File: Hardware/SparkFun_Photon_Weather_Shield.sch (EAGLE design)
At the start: 42 parts, among them U1 3.3V MIC5219, U2 HTU21D, U3 MPL3115A2LGA8

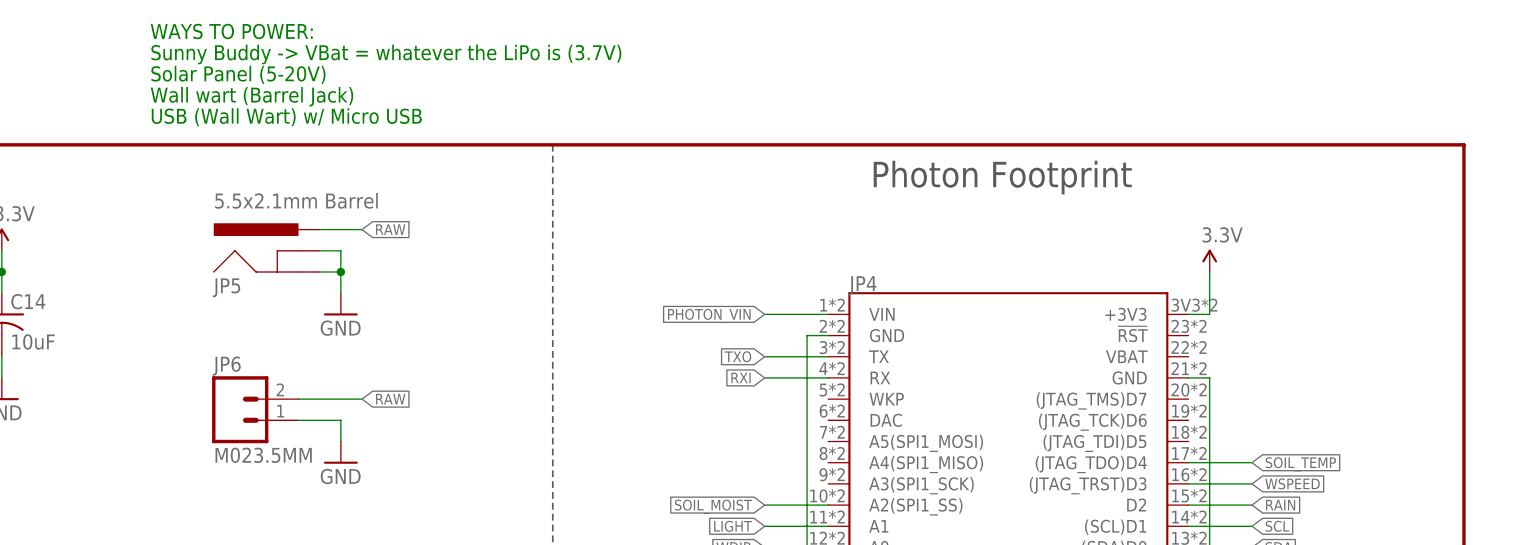
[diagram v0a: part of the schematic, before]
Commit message: Peer Review complete
Peer review with Jim, added 3.3V disable jumper for two power sources
at once (debugging), minor edits.
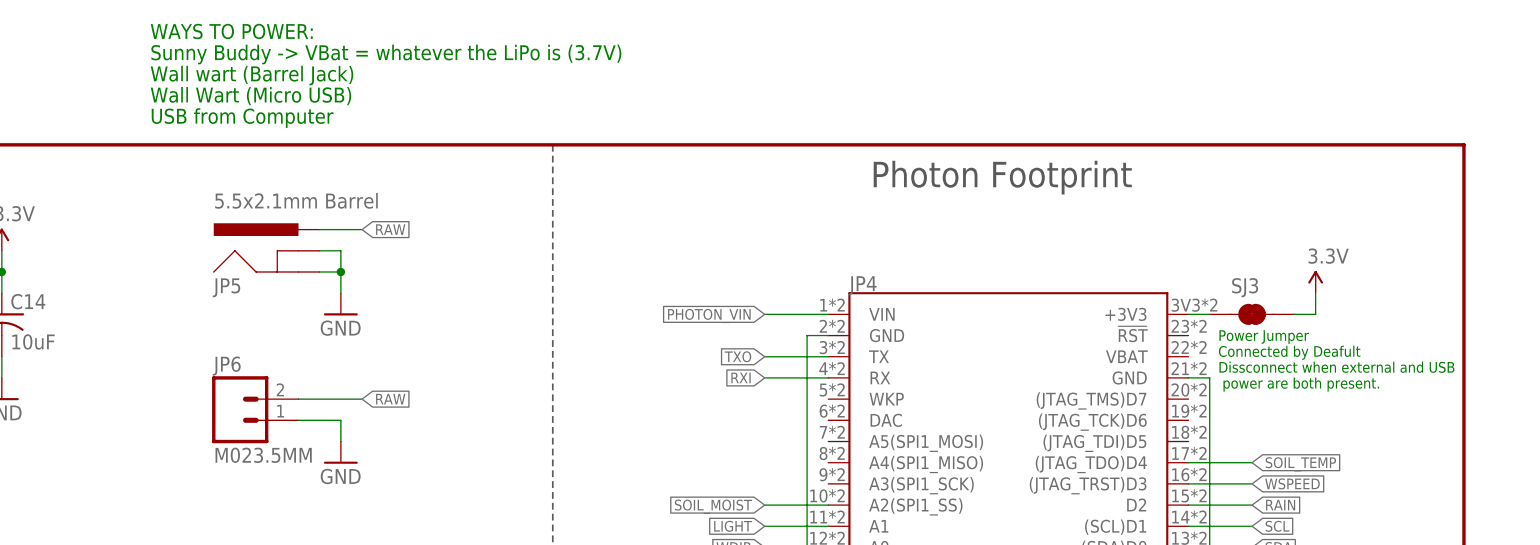
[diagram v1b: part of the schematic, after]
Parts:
- added SJ3: JUMPER-PAD-2-NC_BY_TRACE, SparkFun-Passives:JUMPER-PAD-2-NC_BY_TRACE
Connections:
- new net N$7: JP4.+3V3, SJ3.1
- net 3.3V: now also SJ3.2; no longer JP4.+3V3
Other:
- note added: "Power Jumper Connected by Deafult Dissconnect when external and USB power are both present."
- note added: "USB from Computer"
- note added: "Wall Wart (Micro USB)"
- note removed: "Solar Panel (5-20V)"
- note removed: "USB (Wall Wart) w/ Micro USB"
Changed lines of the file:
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@@
 <part name="FID2" library="SparkFun-Aesthetics" deviceset="FIDUCIAL" device="1X2"/>
 <part name="LOGO2" library="SparkFun-Aesthetics" deviceset="SFE_LOGO_NAME_FLAME" device=".1_INCH"/>
+<part name="SJ3" library="SparkFun-Passives" deviceset="JUMPER-PAD-2-NC_BY_TRACE" device="" value=""/>
 </parts>
 <sheets>
@@
 <text x="96.012" y="36.068" size="2.032" layer="102">I2C Port (optional)</text>
 <text x="91.44" y="195.58" size="1.778" layer="91">Sunny Buddy -&gt; VBat = whatever the LiPo is (3.7V)</text>
-<text x="91.44" y="193.04" size="1.778" layer="91">Solar Panel (5-20V)</text>
-<text x="91.44" y="190.5" size="1.778" layer="91">Wall wart (Barrel Jack)</text>
-<text x="91.44" y="187.96" size="1.778" layer="91">USB (Wall Wart) w/ Micro USB</text>
+<text x="91.44" y="187.96" size="1.778" layer="91">USB from Computer</text>
+<text x="91.44" y="193.04" size="1.778" layer="91">Wall wart (Barrel Jack)</text>
+<text x="91.44" y="190.5" size="1.778" layer="91">Wall Wart (Micro USB)</text>
 <text x="104.14" y="134.62" size="1.778" layer="91">Power Selection</text>
 <text x="91.44" y="198.12" size="1.778" layer="91">WAYS TO POWER:</text>
 <text x="149.86" y="7.62" size="1.778" layer="94" ratio="12">Based on the Weather Shield for Arduino by Nathan Seidle</text>
 <text x="27.94" y="144.78" size="1.778" layer="97">Min Voltage Input: 5VDC</text>
+<text x="219.456" y="156.21" size="1.27" layer="91">Power Jumper
+Connected by Deafult
+Dissconnect when external and USB
+ power are both present. </text>
 </plain>
 <instances>
@@
 </instance>
 <instance part="LOGO1" gate="G$1" x="165.1" y="45.72"/>
-<instance part="P+2" gate="G$1" x="218.44" y="170.18"/>
+<instance part="P+2" gate="G$1" x="231.14" y="167.64"/>
 <instance part="JP2" gate="G$1" x="7.62" y="17.78"/>
 <instance part="JP3" gate="G$1" x="55.88" y="17.78"/>
@@
 <instance part="FID2" gate="G$1" x="243.84" y="25.4"/>
 <instance part="LOGO2" gate="G$1" x="190.5" y="33.02"/>
+<instance part="SJ3" gate="G$1" x="223.52" y="165.1"/>
 </instances>
 <busses>
@@
 </segment>
 <segment>
-<pinref part="P+2" gate="G$1" pin="3.3V"/>
-<wire x1="215.9" y1="165.1" x2="218.44" y2="165.1" width="0.1524" layer="91"/>
-<wire x1="218.44" y1="165.1" x2="218.44" y2="170.18" width="0.1524" layer="91"/>
-<pinref part="JP4" gate="G$1" pin="+3V3"/>
-</segment>
-<segment>
 <pinref part="JP2" gate="G$1" pin="3"/>
 <wire x1="15.24" y1="20.32" x2="17.78" y2="20.32" width="0.1524" layer="91"/>
@@
 <pinref part="R17" gate="G$1" pin="1"/>
 <pinref part="P+14" gate="1" pin="VCC"/>
+</segment>
+<segment>
+<pinref part="SJ3" gate="G$1" pin="2"/>
+<pinref part="P+2" gate="G$1" pin="3.3V"/>
+<wire x1="231.14" y1="167.64" x2="231.14" y2="165.1" width="0.1524" layer="91"/>
+<wire x1="231.14" y1="165.1" x2="228.6" y2="165.1" width="0.1524" layer="91"/>
 </segment>
 </net>
@@
 </segment>
 </net>
+<net name="N$7" class="0">
+<segment>
+<pinref part="SJ3" gate="G$1" pin="1"/>
+<pinref part="JP4" gate="G$1" pin="+3V3"/>
+<wire x1="218.44" y1="165.1" x2="215.9" y2="165.1" width="0.1524" layer="91"/>
+</segment>
+</net>

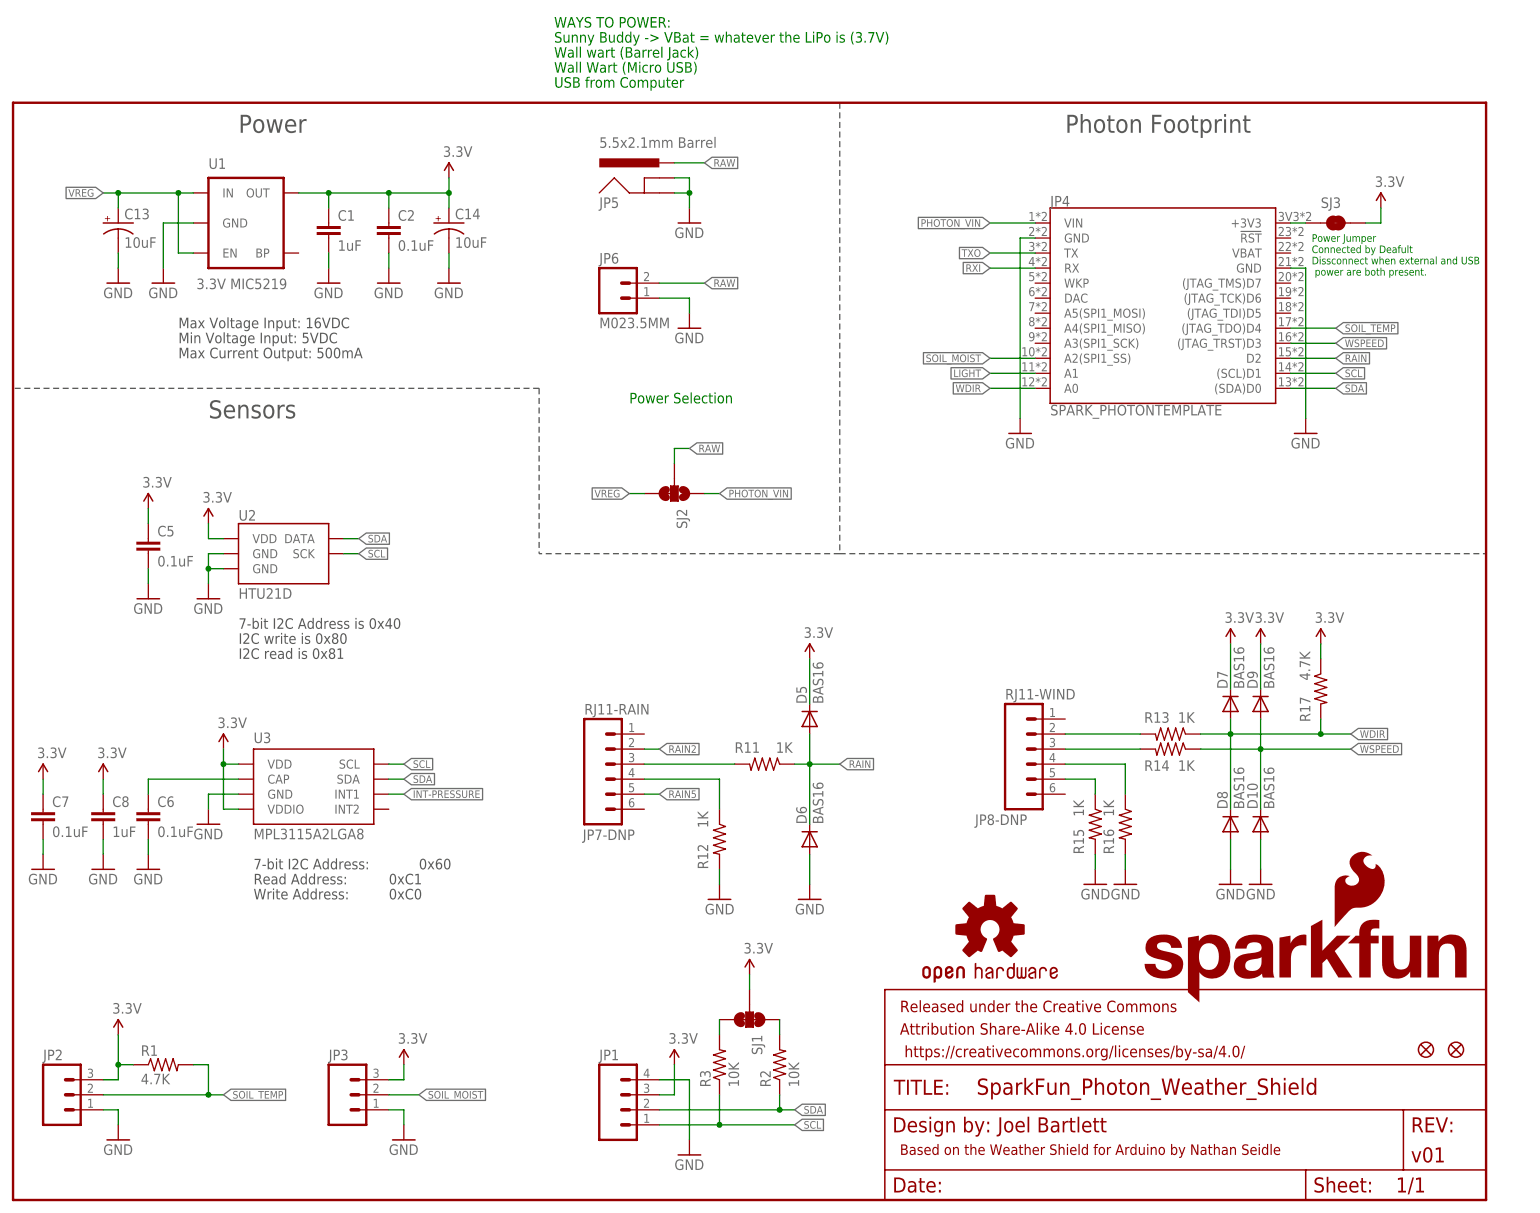
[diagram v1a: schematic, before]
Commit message: Ready for QC Checklist
Replaced all old Eagle parts with most up to date library parts, added
a Dimension Route as well as the Milling Route, Fixed Trestrict and
Restrict, which were on Keepout instead.
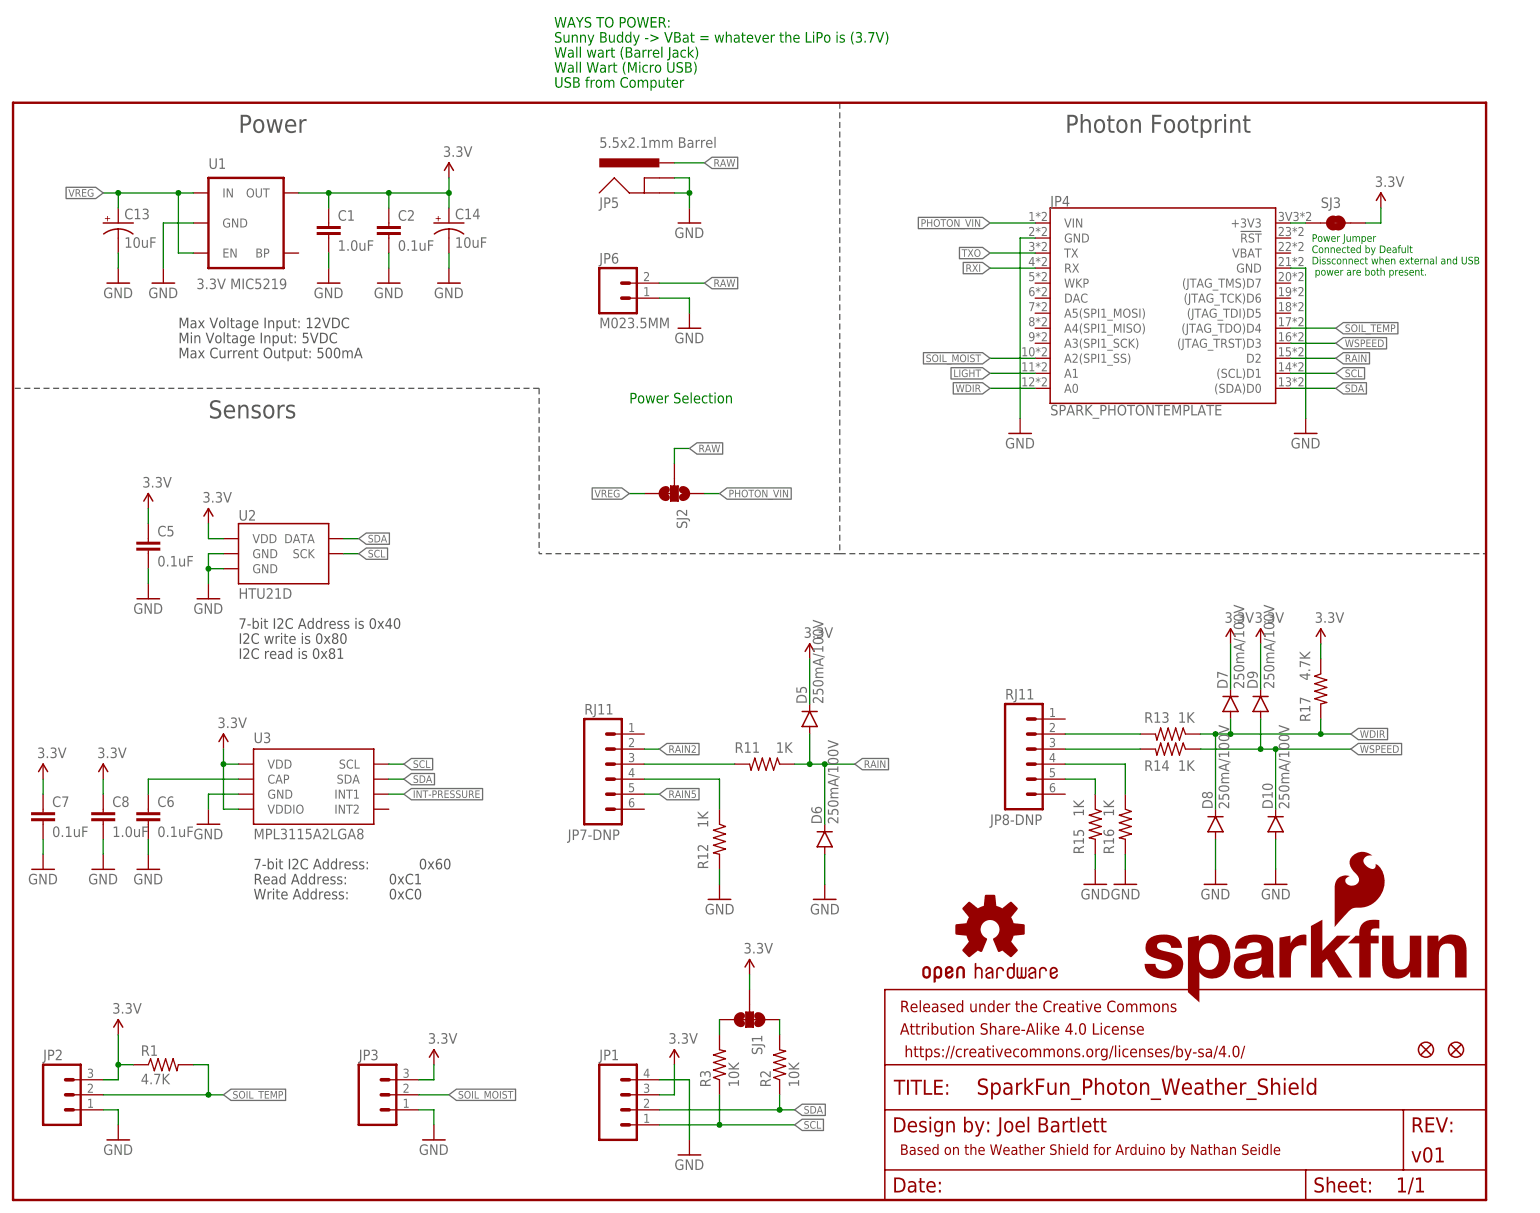
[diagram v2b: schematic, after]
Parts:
- C1, C8: value 1uF -> 1.0uF; device SparkFun:CAP0603-CAP -> SparkFun-Capacitors:1.0UF-16V-10%(0603)
- C13, C14: device SparkFun-Passives:CAP_POL1206 -> SparkFun-Capacitors:10UF-16V-10%(TANT)
- C2, C5, C6, C7: device SparkFun:CAP0603-CAP -> SparkFun-Capacitors:0.1UF-25V(+80/-20%)(0603)
- D10, D5, D6, D7, D8, D9: value BAS16 -> 250mA/100V; device SparkFun:DIODESOD -> SparkFun-DiscreteSemi:DIODEBAS16
- JP7-DNP: value RJ11-RAIN -> RJ11; device SparkFun:RJ11-6PTH -> SparkFun-Connectors:RJ11-6PTH
- JP8-DNP: value RJ11-WIND -> RJ11; device SparkFun:RJ11-6PTH -> SparkFun-Connectors:RJ11-6PTH
- R11, R12, R13, R14, R15, R16: device SparkFun:RESISTOR0603-RES -> SparkFun-Resistors:1KOHM-1/10W-1%(0603)
- R17: device SparkFun:RESISTOR0603-RES -> SparkFun-Resistors:4.7KOHM-1/10W-1%(0603)
- U1: device SparkFun:V_REG_LDOSMD -> SparkFun-PowerIC:MIC52053.3V
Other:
- note added: "Max Voltage Input: 12VDC"
- note removed: "Max Voltage Input: 16VDC"
- moved on the sheet: JP3
